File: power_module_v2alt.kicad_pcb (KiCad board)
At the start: 4 copper layers, 100 x 70 mm, 76 parts, among them J1_BMS1 I2C+ALERT, J1_INPUT1 USB_C_16P, Q1_BMS1 AON7544, Q1_BUCKBOOST1 AON7544, Q2_BMS1 AON7544, Q2_BUCKBOOST1 AON7544, Q3_BUCKBOOST1 AON7544, Q4_BUCKBOOST1 AON7544, U1_BMS1 BQ7692003PWR, U1_BUCKBOOST1 LM5176PWP, U1_CHARGER1 IP2326, U1_INPUT1 CH224K

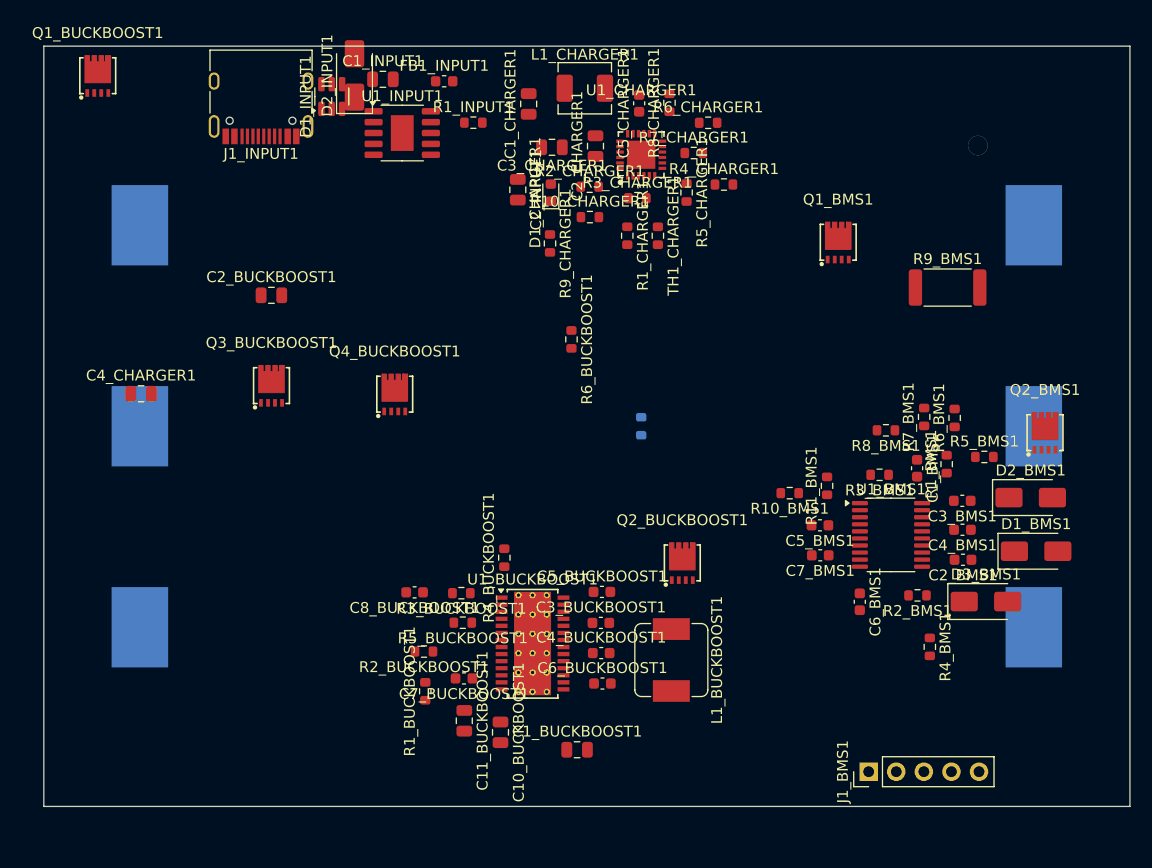
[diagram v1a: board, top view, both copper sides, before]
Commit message: Step 4 complete: SW1 kill switch, buck-boost thermal cluster, second relax pass
Kill switch (SW1_BMS1) added to bms sheet.  SPDT slide (Switch:SW_SPDT
symbol, Button_Switch_SMD:SW_SPDT_PCM12 footprint).  Topology:

  BQ76920.DSG_DRV (pin 1)  ──► SW1.1 (throw ON)
                             ▲
  R10_BMS1.1 ── DSG_DRV_GATED ── SW1.2 (common)
                             ▼
                             SW1.3 (throw OFF) ── GND

When switch is in throw 1 (ON) the DSG_DRV signal reaches R10 and drives
Q1's gate normally.  When in throw 3 (OFF) common shorts to GND and pulls
R10.1 low, which via R10 pulls Q1's gate to GND — the discharge FET turns
off and the pack output goes dead.  Charge path (Q2_BMS1) is unaffected,
so the pack can still be charged through the BMS with the switch off.

DSG_DRV split into DSG_DRV (BQ76920 → SW1.1) and DSG_DRV_GATED (SW1.2 →
R10.1).  Sync + `place_component` used because the retroactive-import gap
in sync_schematic_to_board would otherwise leave the SW1 footprint off
the board.

Buck-boost thermal cluster moved to bottom edge

U1_BUCKBOOST1 (LM5176 HTSSOP-28 with EP thermal pad) and the whole
power stage moved out from under BAT1's projected keepout and down to the
bottom-left corner where the board edge acts as a heatsink:

  U1_BUCKBOOST1   → (30, 58)    LM5176
  Q1_BUCKBOOST1   → (18, 55)    buck HS
  Q2_BUCKBOOST1   → (18, 61)    buck LS
  Q3_BUCKBOOST1   → (42, 61)    boost LS
  Q4_BUCKBOOST1   → (42, 55)    boost HS
  L1_BUCKBOOST1   → (30, 66)    SW1↔SW2 inductor
  C1_BUCKBOOST1   → (12, 58)    Cin bulk 22uF
  C2_BUCKBOOST1   → (12, 65)    Cin bulk 22uF
  C10_BUCKBOOST1  → (48, 65)    Cout bulk 22uF
  C11_BUCKBOOST1  → (48, 58)    Cout bulk 22uF

Second relax_placement pass

18 refs locked (2 headers + BAT1 + TH1 + SW1 + 4 ICs + 10 buck-boost).
Everything else pulled toward its natural cluster.  The META1 singleton's
mcp_spring_classes now takes effect: BAT+/VBUS_9V/VBUS_RAW/VOUT_12V/VSYS
are PLANE-classified and no longer distort 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
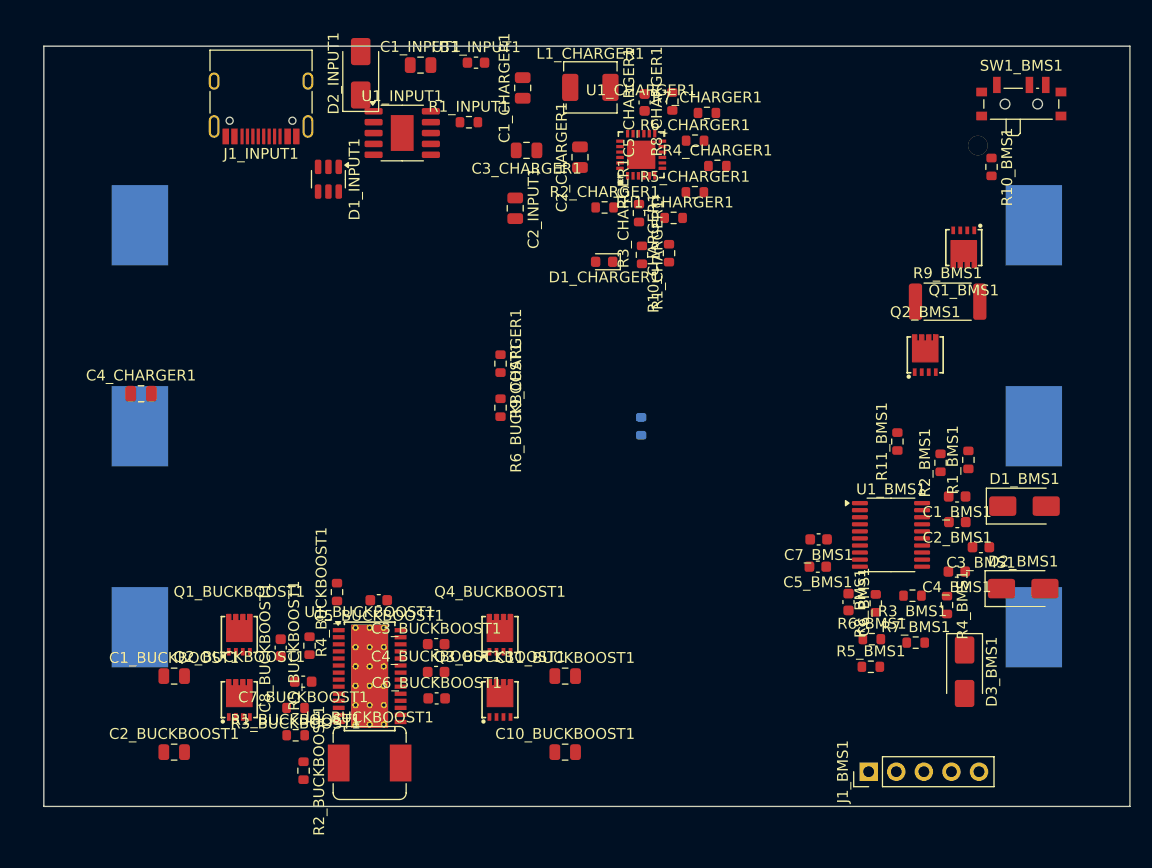
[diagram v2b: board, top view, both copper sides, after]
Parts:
- added SW1_BMS1: Kill Switch, Button_Switch_SMD:SW_SPDT_PCM12, F.Cu at (90.0, 5.00)
- moved Q1_BUCKBOOST1 53.1 mm to (18.0, 55.0)
- moved C2_BUCKBOOST1 43.0 mm to (12.0, 65.0)
- moved Q2_BUCKBOOST1 42.7 mm to (18.0, 61.0)
- moved C1_BUCKBOOST1 37.7 mm to (12.0, 58.0)
- moved Q3_BUCKBOOST1 35.8 mm to (42.0, 61.0)
- moved R10_BMS1 35.3 mm to (87.3, 11.1), turned to -90 degrees
- moved L1_BUCKBOOST1 29.4 mm to (30.0, 66.0), turned to 0 degrees
- moved Q4_BUCKBOOST1 24.2 mm to (42.0, 55.0)
- moved R5_BMS1 22.0 mm to (76.1, 57.1)
- moved R6_BMS1 21.7 mm to (76.2, 54.6), turned to 0 degrees
- moved R7_BMS1 20.8 mm to (80.3, 54.9), turned to 0 degrees
- moved C5_BUCKBOOST1 20.6 mm to (30.8, 51.0), turned to 180 degrees
- moved R3_BUCKBOOST1 18.6 mm to (23.2, 60.9)
- moved R8_BMS1 16.0 mm to (76.6, 51.3), turned to 90 degrees
- moved R4_BUCKBOOST1 15.7 mm to (27.0, 50.3)
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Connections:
- R10_BMS1 pad 1: DSG_DRV -> DSG_DRV_GATED
